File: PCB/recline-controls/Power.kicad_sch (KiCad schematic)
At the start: 8 parts, among them J4 1757242, M1 D24V22F5, M2 D24V22F3

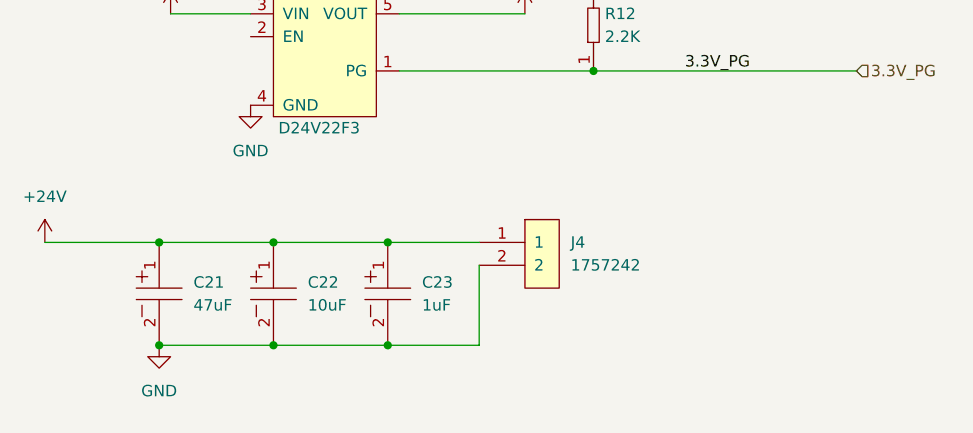
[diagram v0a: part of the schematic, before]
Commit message: All Hardware Tweaked / 3D Renders
PCBs for Actuator Control, Recline Control HID, and 7 Segment carrier are all complete with full 3D models rendering. 3D Renders of all board added to repository img directory.
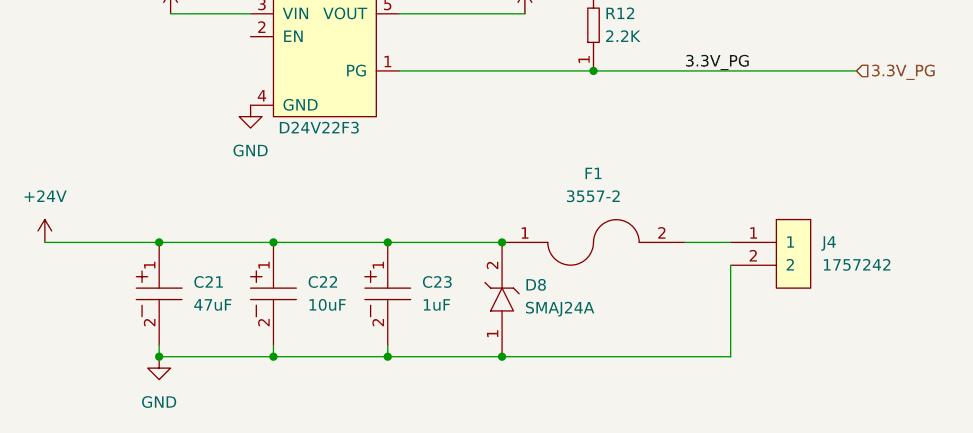
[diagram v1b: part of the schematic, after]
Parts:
- added D8: SMAJ24A, AVR-KiCAD-Lib-Diodes:SMAJ, symbol AVR-KiCAD-Lib-Diodes:SMAJ24A
- added F1: 3557-2, AVR-KiCAD-Lib-Fuse-Holders:FUSE_3557-2, symbol AVR-KiCAD-Lib-Fuse-Holders:3557-2
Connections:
- net +24V: now also D8.2, F1.1; no longer J4.1
- net GND: now also D8.1
- new net: F1.2, J4.1
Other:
- moved on the sheet: J4

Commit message: HID
Changes made to recline control HID board. Power input section redesigned, 5V regulator removed, RS485 circuit updated with fixes that other boards received. Redesign or internal plane topology following changes to RS485 section. Via stitching all around.
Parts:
- removed M1: D24V22F5, AVR-KiCAD-Lib-Modules:D24V22F12, symbol AVR-KiCAD-Lib-Modules:D24V22F5
- removed R11: RC0603FR-072K2L, AVR-KiCAD-Lib-Resistors:R0603, symbol AVR-KiCAD-Lib-Resistors:RC0603FR-072K2L
